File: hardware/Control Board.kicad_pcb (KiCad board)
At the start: 2 copper layers, 68.4 x 53.1 mm, 46 parts, among them J1 Conn_FTDI, J2 SOLAR, M1 MOTOR, Q1 IRF7105PbF, Q2 BC817W, Q3 BC817W, Q4 IRF7105PbF, SW1 SW_Push, SW2 SW_Push, SW3 SW_Push, SW4 SW_Push, SW5 SW_Push, SW6 SW_Push, U1 BQ24075, U2 MCP1700, U3 ESP32S2-WROVER

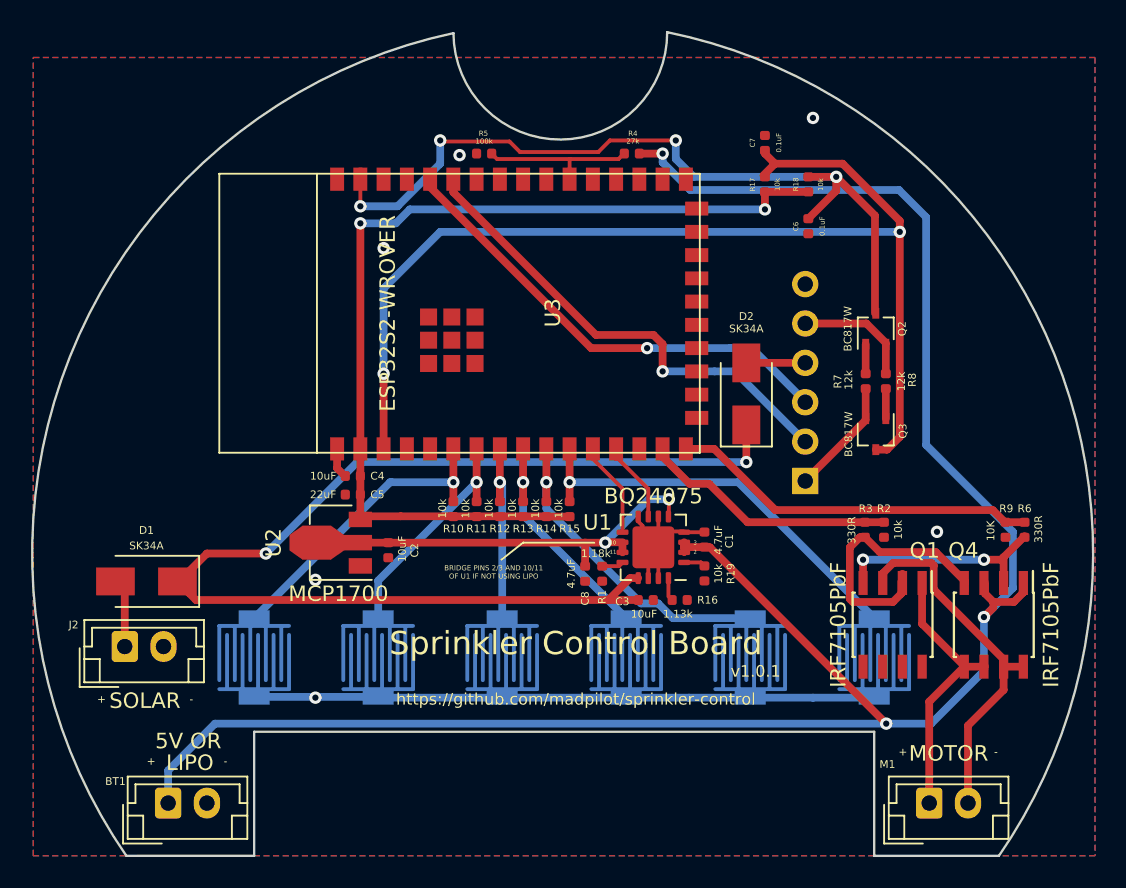
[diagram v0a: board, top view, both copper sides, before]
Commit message: Copying board from firmware/powered
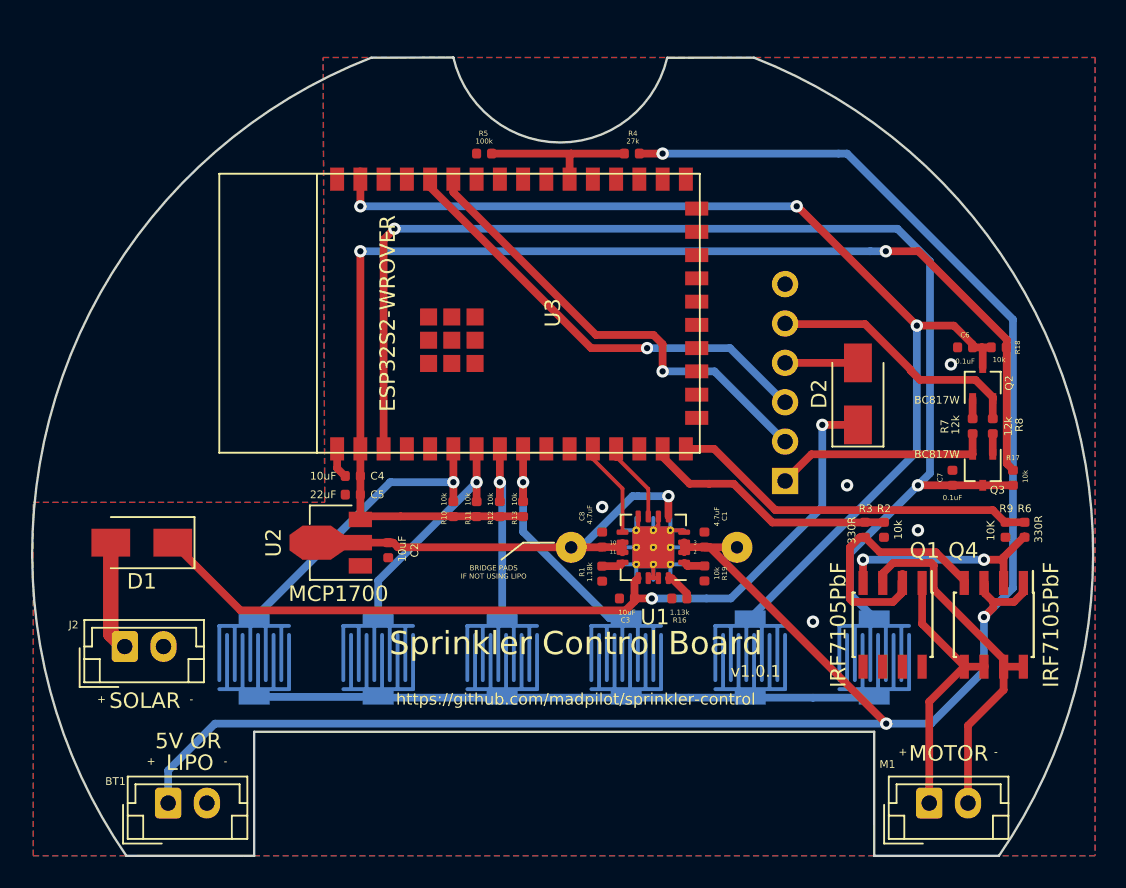
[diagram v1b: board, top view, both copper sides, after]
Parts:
- removed R14, R15: 10k, Resistor_SMD:R_0402_1005Metric
- added REF**: SolderWirePad_1x01_Drill0.8mm, Connector_Wire:SolderWirePad_1x01_Drill0.8mm, F.Cu at (120.4, 130.1)
- added REF**: SolderWirePad_1x01_Drill0.8mm, Connector_Wire:SolderWirePad_1x01_Drill0.8mm, F.Cu at (109.7, 130.1)
- PROG: renamed from SW1; value SW_Push -> PROG
- RESET: renamed from SW2; value SW_Push -> RESET
- U1: footprint Package_DFN_QFN:Texas_S-PVQFN-N16_EP2.7x2.7mm -> Package_DFN_QFN:Texas_S-PVQFN-N16_EP2.7x2.7mm_ThermalVias
- moved R17 24.8 mm to (138.2, 125.6), turned to 270 degrees
- moved C7 24.8 mm to (134.3, 125.6)
- moved R18 16.2 mm to (137.3, 117.2), turned to 180 degrees
- moved C6 12.8 mm to (135.1, 117.2), turned to 180 degrees
- moved Q2 7.74 mm to (136.2, 119.5)
- moved R7 7.48 mm to (135.6, 122.3)
- moved R8 7.48 mm to (136.9, 122.3)
- moved Q3 7.27 mm to (136.2, 125.1)
- moved D2 7.20 mm to (128.2, 120.2)
- moved D1 2.52 mm to (82.0, 129.8)
- moved C8 2.46 mm to (111.7, 129.6), turned to 90 degrees
- moved J1 1.30 mm to (123.5, 125.8)
- moved C3 1.21 mm to (113.3, 133.4), turned to 0 degrees
- moved R16 0.10 mm to (116.7, 133.4), turned to 180 degrees
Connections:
- PROG pad 2: Net-(R15-Pad2) -> IO0
- RESET pad 2: Net-(R14-Pad2) -> EN
- U3 pad 10: Net-(R14-Pad2) -> Net-(U3-Pad10)
- U3 pad 11: Net-(R15-Pad2) -> Net-(U3-Pad11)
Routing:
- net Net-(R15-Pad2): track 26.7 -> 0.00 mm, vias 1 -> 0
- net Net-(R14-Pad2): track 21.1 -> 0.00 mm, vias 1 -> 0
- net Net-(C3-Pad2): track 76.0 -> 55.6 mm
- net EN: track 53.0 -> 71.4 mm, vias 4 -> 3
- net +3V3: track 63.0 -> 81.1 mm
- net GND: track 55.4 -> 67.0 mm, vias 6 -> 5
- net Net-(J1-Pad5): track 7.62 -> 16.8 mm
- net IO0: track 72.7 -> 81.8 mm
- net Net-(J1-Pad1): track 7.47 -> 14.1 mm
- net Net-(D1-Pad2): track 4.35 -> 8.16 mm
- net RX: track 31.2 -> 29.9 mm
- net TX: track 30.9 -> 29.6 mm
- net +BATT: track 134.6 -> 135.7 mm
- net Net-(C2-Pad1): track 29.3 -> 30.4 mm, vias 2 -> 1
- net +5V: track 3.80 -> 4.70 mm
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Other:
- board size 68.4 x 53.1 mm -> 68.4 x 51.5 mm
- board text added: "3V3"
- board text added: "BRIDGE PADS IF NOT USING LIPO"
- board text removed: "5V"
- board text removed: "BRIDGE PINS 2/3 AND 10/11 OF U1 IF NOT USING LIPO"

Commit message: Routing MOSFETs
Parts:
- removed the C7 at (134.3, 125.6)
- removed the Q2 at (136.2, 119.5)
- removed the R16 at (116.7, 133.4)
- removed the R19 at (118.3, 131.8)
- removed the R6 at (138.9, 129.0)
- removed REF** (x2): SolderWirePad_1x01_Drill0.8mm, Connector_Wire:SolderWirePad_1x01_Drill0.8mm
- added C4: 10uF, Capacitor_SMD:C_0805_2012Metric, F.Cu at (95.7, 130.6)
- added Q1: BC817W, Package_TO_SOT_SMD:SOT-323_SC-70, F.Cu at (139.2, 132.2)
- added Q3: BC817W, Package_TO_SOT_SMD:SOT-323_SC-70, F.Cu at (131.6, 125.1)
- added Q6: BC817W, Package_TO_SOT_SMD:SOT-323_SC-70, F.Cu at (122.0, 132.2)
- added R17: 330R, Resistor_SMD:R_0805_2012Metric, F.Cu at (122.9, 138.2)
- added R2: 1.13k, Resistor_SMD:R_0805_2012Metric, F.Cu at (114.4, 133.5)
- added R3: 10k, Resistor_SMD:R_0805_2012Metric, F.Cu at (116.3, 133.5)
- added R5: 10k, Resistor_SMD:R_0805_2012Metric, F.Cu at (103.4, 128.2)
- added R9: 10k, Resistor_SMD:R_0805_2012Metric, F.Cu at (107.2, 128.2)
- C1: value 4.7uF -> 10uF; footprint Capacitor_SMD:C_0402_1005Metric -> Capacitor_SMD:C_0805_2012Metric
- C2, C3: value 10uF -> 4.7uF; footprint Capacitor_SMD:C_0402_1005Metric -> Capacitor_SMD:C_0805_2012Metric
- C5: footprint Capacitor_SMD:C_0402_1005Metric -> Capacitor_SMD:C_0805_2012Metric
- C6: renamed from C4; footprint Capacitor_SMD:C_0402_1005Metric -> Capacitor_SMD:C_0805_2012Metric
- C7: renamed from C6; footprint Capacitor_SMD:C_0402_1005Metric -> Capacitor_SMD:C_0805_2012Metric
- C8: value 4.7uF -> 0.1uF; footprint Capacitor_SMD:C_0402_1005Metric -> Capacitor_SMD:C_0805_2012Metric
- R1, R11, R13, R18: footprint Resistor_SMD:R_0402_1005Metric -> Resistor_SMD:R_0805_2012Metric
- R10: renamed from R2; footprint Resistor_SMD:R_0402_1005Metric -> Resistor_SMD:R_0805_2012Metric
- R12: renamed from R3; footprint Resistor_SMD:R_0402_1005Metric -> Resistor_SMD:R_0805_2012Metric
- R14: renamed from R17; footprint Resistor_SMD:R_0402_1005Metric -> Resistor_SMD:R_0805_2012Metric
- R15: renamed from R7; footprint Resistor_SMD:R_0402_1005Metric -> Resistor_SMD:R_0805_2012Metric
- R16: renamed from R8; footprint Resistor_SMD:R_0402_1005Metric -> Resistor_SMD:R_0805_2012Metric
- R19: renamed from R9; footprint Resistor_SMD:R_0402_1005Metric -> Resistor_SMD:R_0805_2012Metric
- R4: renamed from R10; footprint Resistor_SMD:R_0402_1005Metric -> Resistor_SMD:R_0805_2012Metric
- R6: renamed from R12; footprint Resistor_SMD:R_0402_1005Metric -> Resistor_SMD:R_0805_2012Metric
- R7: renamed from R4; footprint Resistor_SMD:R_0402_1005Metric -> Resistor_SMD:R_0805_2012Metric
- R8: renamed from R5; footprint Resistor_SMD:R_0402_1005Metric -> Resistor_SMD:R_0805_2012Metric
- moved R13 29.6 mm to (136.1, 125.1), turned to 270 degrees
- moved C8 27.5 mm to (134.2, 113.8), turned to 270 degrees
- moved R11 25.0 mm to (128.3, 131.5), turned to 0 degrees
- moved C2 18.5 mm to (116.3, 128.2), turned to 90 degrees
- moved R18 15.0 mm to (132.8, 131.5)
- moved R12 13.4 mm to (138.3, 138.2)
- moved R19 13.0 mm to (124.9, 131.5), turned to 180 degrees
- moved R16 12.6 mm to (128.2, 113.1), turned to 0 degrees
- moved Q4 12.2 mm to (131.6, 113.9), turned to 90 degrees
- moved R14 12.0 mm to (136.1, 113.8), turned to 90 degrees
- moved C1 8.22 mm to (111.1, 133.5)
- moved R15 8.20 mm to (128.2, 125.8), turned to 0 degrees
- moved C7 7.94 mm to (134.2, 125.1), turned to 90 degrees
- moved R10 6.84 mm to (136.2, 131.5), turned to 180 degrees
- moved C3 6.67 mm to (109.1, 128.2), turned to 90 degrees
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- renumbered J2 to J1, J1 to J2, Q1 to Q2, Q3 to Q4, Q4 to Q5, PROG to SW1, RESET to SW2
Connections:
- C1 pad 1: +BATT -> GND
- C1 pad 2: GND -> Net-(C1-Pad2)
- C2 pad 1: Net-(C2-Pad1) -> +BATT
- C3 pad 1: GND -> Net-(C3-Pad1)
- C3 pad 2: Net-(C3-Pad2) -> GND
- C8 pad 1: Net-(C2-Pad1) -> IO0
- D1 pad 1: Net-(C3-Pad2) -> Net-(C1-Pad2)
- D2 pad 1: Net-(C3-Pad2) -> Net-(C1-Pad2)
- M1 pad 1: M+ -> Net-(M1-Pad1)
- M1 pad 2: M- -> Net-(M1-Pad2)
- Q2 pad 1: M+ -> GND
- Q2 pad 2: Net-(Q1-Pad2) -> WATER_OFF
- Q2 pad 3: M- -> +BATT
- Q2 pad 4: Net-(Q1-Pad4) -> Net-(Q1-Pad3)
- Q2 pad 5: GND -> Net-(M1-Pad1)
- Q2 pad 6: GND -> Net-(M1-Pad1)
- Q2 pad 7: GND -> Net-(M1-Pad1)
- Q2 pad 8: GND -> Net-(M1-Pad1)
- Q5 pad 1: +BATT -> GND
- Q5 pad 2: Net-(Q1-Pad4) -> WATER_ON
- Q5 pad 3: +BATT -> Net-(Q5-Pad3)
- Q5 pad 4: Net-(Q1-Pad2) -> Net-(Q5-Pad4)
- Q5 pad 5: M+ -> Net-(M1-Pad2)
- Q5 pad 6: M+ -> Net-(M1-Pad2)
- Q5 pad 7: M- -> Net-(M1-Pad2)
- Q5 pad 8: M- -> Net-(M1-Pad2)
- R10 pad 1: WATER_ON -> Net-(Q1-Pad1)
- R10 pad 2: GND -> WATER_ON
- R11 pad 1: +3V3 -> WATER_OFF
- R11 pad 2: Net-(R11-Pad2) -> GND
- R12 pad 1: Net-(Q1-Pad2) -> +BATT
- R12 pad 2: WATER_ON -> Net-(Q1-Pad3)
- R13 pad 2: Net-(R13-Pad2) -> EN
- R18 pad 1: +3V3 -> WATER_ON
- R18 pad 2: EN -> GND
- R19 pad 2: GND -> Net-(Q6-Pad1)
- SW3 pad 2: Net-(R13-Pad2) -> Net-(R9-Pad2)
- SW5 pad 2: Net-(R11-Pad2) -> Net-(R5-Pad2)
- U1 pad 10: Net-(C2-Pad1) -> Net-(C3-Pad1)
- U1 pad 11: Net-(C2-Pad1) -> Net-(C3-Pad1)
- U1 pad 13: Net-(C3-Pad2) -> Net-(C1-Pad2)
- U1 pad 5: Net-(C2-Pad1) -> Net-(C3-Pad1)
- U2 pad 2: Net-(C2-Pad1) -> Net-(C3-Pad1)
- U3 pad 15: WATER_ON -> WATER_OFF
- U3 pad 16: WATER_OFF -> WATER_ON
- U3 pad 7: Net-(R11-Pad2) -> Net-(R5-Pad2)
- U3 pad 9: Net-(R13-Pad2) -> Net-(R9-Pad2)
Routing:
- net IO0: track 81.8 -> 150.5 mm
- net Net-(C1-Pad2): track 0.00 -> 61.0 mm, vias 0 -> 2
- net Net-(C3-Pad2): track 55.6 -> 0.00 mm, vias 2 -> 0
- net Net-(C3-Pad1): track 0.00 -> 31.1 mm, vias 0 -> 2
- net Net-(C2-Pad1): track 30.4 -> 0.00 mm, vias 1 -> 0
- net M-: track 23.5 -> 0.00 mm
- net Net-(Q1-Pad3): track 0.00 -> 22.0 mm, vias 0 -> 2
- net +BATT: track 135.7 -> 114.9 mm, vias 3 -> 4
- net Net-(Q5-Pad4): track 0.00 -> 20.3 mm, vias 0 -> 2
- net Net-(Q1-Pad2): track 17.9 -> 0.00 mm
- net M+: track 17.6 -> 0.00 mm
- net Net-(R9-Pad2): track 0.00 -> 15.9 mm, vias 0 -> 1
- net Net-(R13-Pad2): track 15.5 -> 0.00 mm, vias 1 -> 0
- net Net-(R5-Pad2): track 0.00 -> 15.0 mm, vias 0 -> 1
- net Net-(R11-Pad2): track 14.8 -> 0.00 mm, vias 1 -> 0
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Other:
- board text removed: "10"
- board text removed: "11"
- board text removed: "2"
- board text removed: "3"

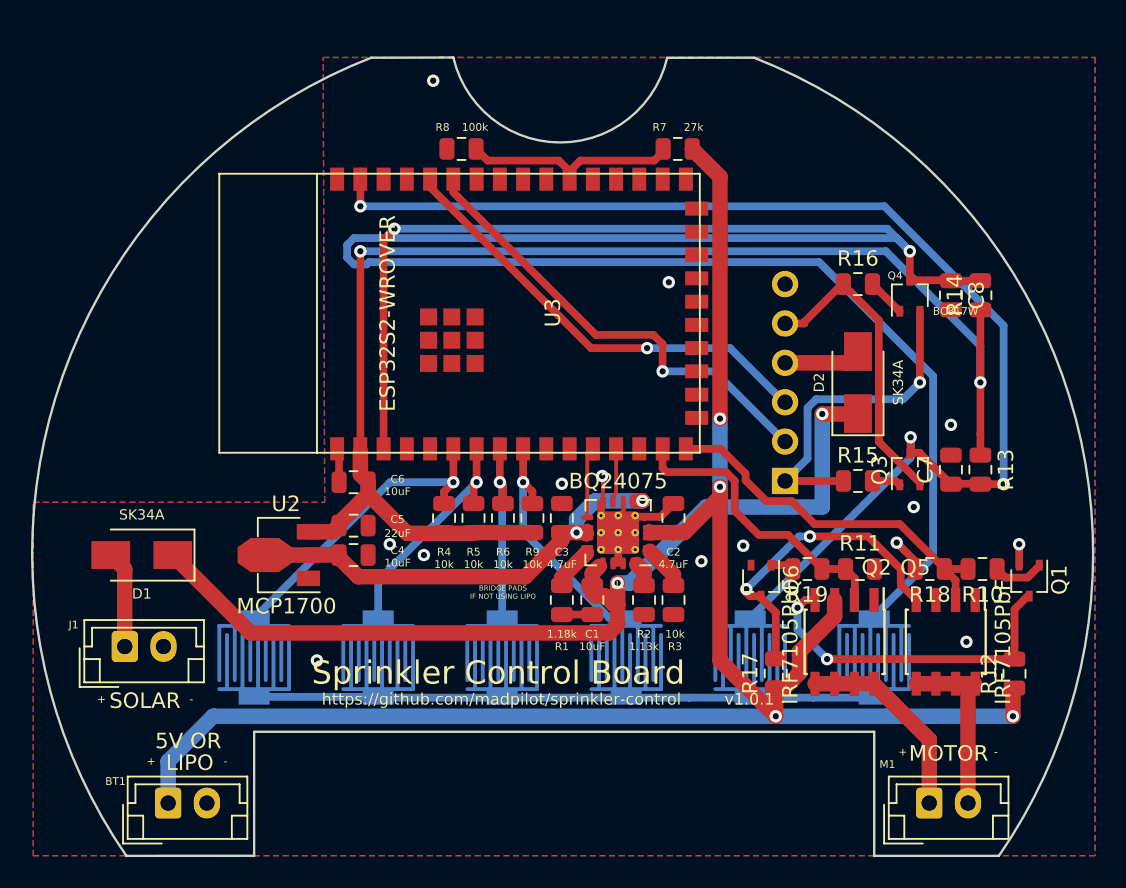
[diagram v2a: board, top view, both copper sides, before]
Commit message: Adding mounting holes
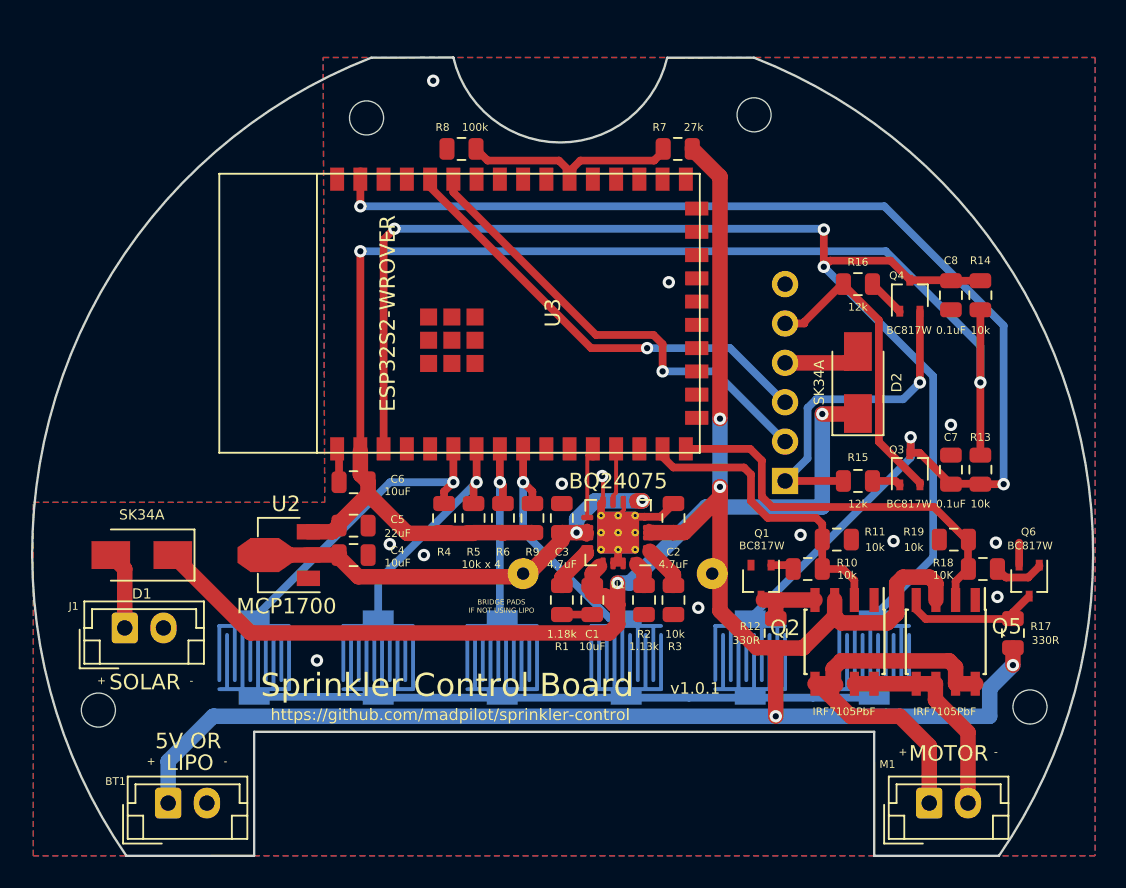
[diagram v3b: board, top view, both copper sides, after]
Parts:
- added REF**: MountingHole_2.2mm_M2, MountingHole:MountingHole_2.2mm_M2, F.Cu at (96.5, 102.4)
- added REF**: MountingHole_2.2mm_M2, MountingHole:MountingHole_2.2mm_M2, F.Cu at (121.5, 102.2)
- added REF**: MountingHole_2.2mm_M2, MountingHole:MountingHole_2.2mm_M2, F.Cu at (79.2, 140.6)
- added REF**: MountingHole_2.2mm_M2, MountingHole:MountingHole_2.2mm_M2, F.Cu at (139.3, 140.4)
- added REF**: SolderWirePad_1x01_Drill0.8mm, Connector_Wire:SolderWirePad_1x01_Drill0.8mm, F.Cu at (118.8, 131.8)
- added REF**: SolderWirePad_1x01_Drill0.8mm, Connector_Wire:SolderWirePad_1x01_Drill0.8mm, F.Cu at (106.6, 131.8)
- R5: value 10k -> 10k x 4
- moved Q1 17.3 mm to (122.0, 132.2)
- moved Q6 17.3 mm to (139.2, 132.2)
- moved R12 15.6 mm to (122.9, 135.6)
- moved R17 15.5 mm to (138.2, 135.6)
- moved R19 11.3 mm to (136.3, 131.5), turned to 0 degrees
- moved R10 11.3 mm to (125.0, 131.5), turned to 0 degrees
- moved R18 2.45 mm to (134.4, 129.6)
- moved R11 2.42 mm to (126.8, 129.6)
- moved J1 1.20 mm to (80.9, 135.3)
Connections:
- Q2 pad 7: Net-(M1-Pad1) -> Net-(M1-Pad2)
- Q2 pad 8: Net-(M1-Pad1) -> Net-(M1-Pad2)
- Q5 pad 3: Net-(Q5-Pad3) -> +BATT
- Q5 pad 7: Net-(M1-Pad2) -> Net-(M1-Pad1)
- Q5 pad 8: Net-(M1-Pad2) -> Net-(M1-Pad1)
- R10 pad 2: WATER_ON -> WATER_OFF
- R19 pad 1: WATER_OFF -> WATER_ON
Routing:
- net IO0: track 150.5 -> 82.5 mm, vias 2 -> 3
- net Net-(Q1-Pad3): track 22.0 -> 4.61 mm, vias 2 -> 0
- net Net-(M1-Pad1): track 13.1 -> 25.3 mm
- net Net-(Q5-Pad4): track 20.3 -> 8.87 mm, vias 2 -> 0
- net +BATT: track 114.9 -> 124.0 mm
- net WATER_ON: track 23.7 -> 26.3 mm
- net Net-(M1-Pad2): track 11.6 -> 14.0 mm
- net GND: track 56.9 -> 54.8 mm, vias 14 -> 13
- net Net-(Q6-Pad1): track 1.40 -> 3.31 mm
- net Net-(Q1-Pad1): track 3.26 -> 1.50 mm
- net Net-(D1-Pad2): track 6.27 -> 5.07 mm
- net WATER_OFF: track 19.8 -> 20.8 mm
